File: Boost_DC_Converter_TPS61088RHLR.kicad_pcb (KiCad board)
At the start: 2 copper layers, 1 part, among them U1 TPS61088RHLR

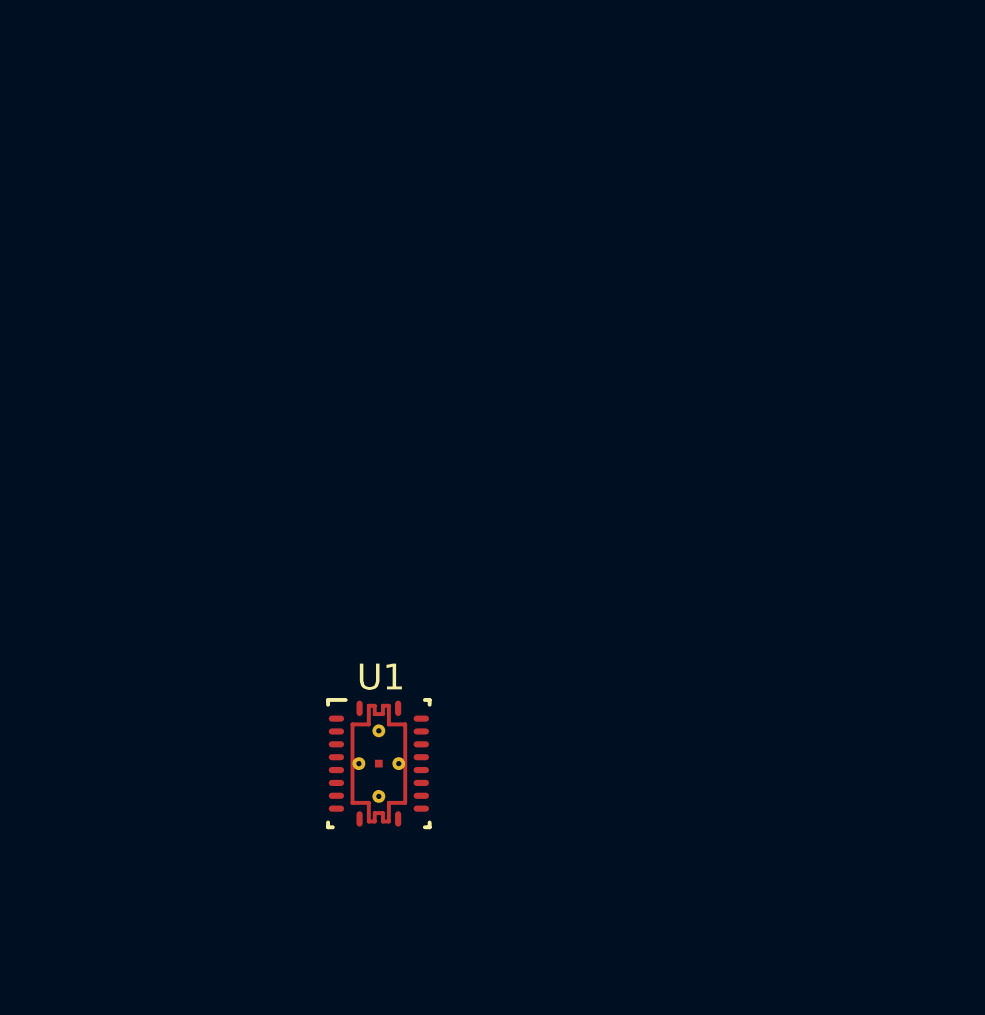
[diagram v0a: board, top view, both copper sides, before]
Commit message: Schematic done
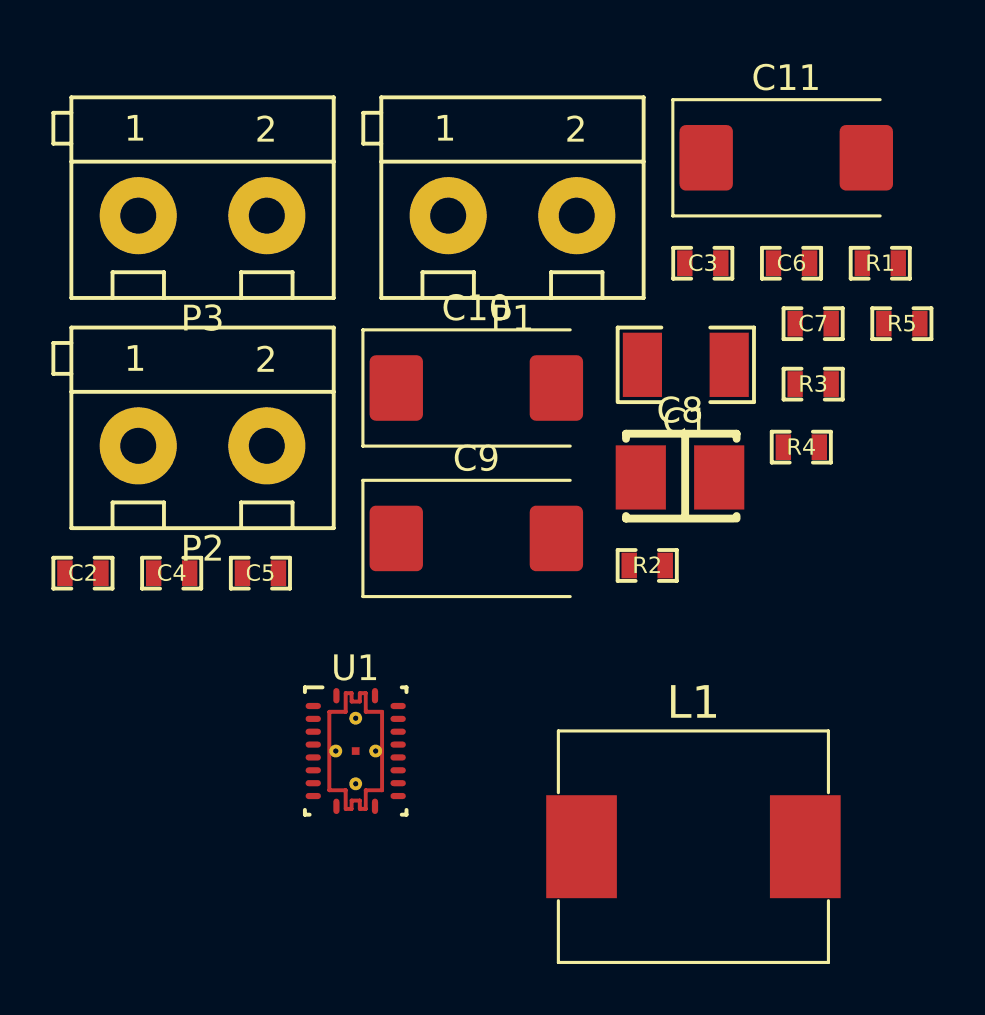
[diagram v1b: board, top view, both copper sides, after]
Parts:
- added C1: 10uF/35V, Capacitors_Smd_1210:10uF_35V_X7R_1210, F.Cu at (160.8, 83.5)
- added C10: 22uF/35V, Smd_Tantal:22uF_35V_Size_D, F.Cu at (152.6, 84.4)
- added C11: 22uF/35V, Smd_Tantal:22uF_35V_Size_D, F.Cu at (164.7, 75.5)
- added C2: 100nF/50V, Capacitors_Smd_0603:100nF_0603, F.Cu at (137.3, 91.6)
- added C3: 2n2F/50V, Capacitors_Smd_0603:2.2nF_0603, F.Cu at (161.4, 79.6)
- added C4: 220pF/50V, Capacitors_Smd_0603:220pF_0603, F.Cu at (140.8, 91.6)
- added C5: 47nF/50V, Capacitors_Smd_0603:47nF_0603, F.Cu at (144.2, 91.6)
- added C6: 2.2uF/6.3V, Capacitors_Smd_0603:2_2uF_0603, F.Cu at (164.9, 79.6)
- added C7: 100nF/50V, Capacitors_Smd_0603:100nF_0603, F.Cu at (165.7, 81.9)
- added C8: 1uF/35V, Smd_Tantal:1uF_35V_B_Tantal, F.Cu at (160.6, 87.9)
- added C9: 22uF/35V, Smd_Tantal:22uF_35V_Size_D, F.Cu at (152.6, 90.3)
- added L1: 1.2uH-12.9A, Inductors:CDMC8D28NP-1R2MC, F.Cu at (161.1, 102.2)
- added P1: DG301-5.0-02P-12-00A(H), Discrete_Connectors:DG301-5.0-02P-12-00A(H), F.Cu at (154.0, 77.7)
- added P2: DG301-5.0-02P-12-00A(H), Discrete_Connectors:DG301-5.0-02P-12-00A(H), F.Cu at (142.0, 86.7)
- added P3: DG301-5.0-02P-12-00A(H), Discrete_Connectors:DG301-5.0-02P-12-00A(H), F.Cu at (142.0, 77.7)
- added R1: 100k, Resistor_Smd_0603:100k_0603, F.Cu at (168.3, 79.6)
- added R2: 100k, Resistor_Smd_0603:100k_0603, F.Cu at (159.3, 91.3)
- added R3: 255k, Resistor_Smd_0603:255k_0603, F.Cu at (165.7, 84.3)
- added R4: 360k, Resistor_Smd_0603:360k_0603, F.Cu at (165.3, 86.7)
- added R5: 56k, Resistor_Smd_0603:56k_0603, F.Cu at (169.2, 81.9)
- moved U1 1.02 mm to (147.9, 98.5)
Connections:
- U1 pad 1: (no net) -> Net-(C6-Pad1)
- U1 pad 10: (no net) -> Net-(C5-Pad1)
- U1 pad 14: (no net) -> Net-(C10-Pad1)
- U1 pad 15: (no net) -> Net-(C10-Pad1)
- U1 pad 16: (no net) -> Net-(C10-Pad1)
- U1 pad 17: (no net) -> Net-(R4-Pad2)
- U1 pad 18: (no net) -> Net-(C4-Pad1)
- U1 pad 19: (no net) -> Net-(R2-Pad1)
- U1 pad 2: (no net) -> Net-(P2-Pad2)
- U1 pad 20: (no net) -> GND
- U1 pad 21: (no net) -> GND
- U1 pad 3: (no net) -> Net-(R3-Pad1)
- U1 pad 4: (no net) -> Net-(C7-Pad2)
- U1 pad 5: (no net) -> Net-(C7-Pad2)
- U1 pad 6: (no net) -> Net-(C7-Pad2)
- U1 pad 7: (no net) -> Net-(C7-Pad2)
- U1 pad 8: (no net) -> Net-(C7-Pad1)
- U1 pad 9: (no net) -> Net-(C1-Pad1)

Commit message: PCB almost done
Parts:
- added MH1: Mounting_Hole_M3_Grounded, Mounting_Holes:Mounting_Hole_M3_Grounded, F.Cu at (134.6, 56.9)
- added MH2: Mounting_Hole_M3_Grounded, Mounting_Holes:Mounting_Hole_M3_Grounded, F.Cu at (178.8, 56.9)
- added MH3: Mounting_Hole_M3_Grounded, Mounting_Holes:Mounting_Hole_M3_Grounded, F.Cu at (134.6, 40.0)
- added MH4: Mounting_Hole_M3_Grounded, Mounting_Holes:Mounting_Hole_M3_Grounded, F.Cu at (178.8, 40.1)
- moved C2 58.6 mm to (165.1, 40.0), turned to 90 degrees
- moved L1 53.0 mm to (169.8, 50.0), turned to 270 degrees
- moved U1 51.7 mm to (161.0, 48.5), turned to 180 degrees
- moved C5 49.5 mm to (160.9, 45.1), turned to 180 degrees
- moved C1 43.6 mm to (162.2, 40.0), turned to 90 degrees
- moved C9 42.0 mm to (149.3, 48.4), turned to 270 degrees
- moved C4 41.9 mm to (155.5, 52.4), turned to 270 degrees
- moved C8 41.6 mm to (153.7, 46.8), turned to 90 degrees
- moved R2 39.0 mm to (158.3, 52.4), turned to 270 degrees
- moved R4 38.8 mm to (157.8, 48.6), turned to 270 degrees
- moved P3 38.7 mm to (144.2, 39.1), turned to 180 degrees
- moved P1 38.6 mm to (154.2, 39.1), turned to 180 degrees
- moved C10 38.5 mm to (138.8, 48.5), turned to 270 degrees
- moved R5 35.7 mm to (156.2, 48.6), turned to 90 degrees
- moved C7 34.7 mm to (164.2, 47.3), turned to 270 degrees
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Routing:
- net GND: track 0.00 -> 77.6 mm, vias 0 -> 1
- net Net-(C7-Pad2): track 0.00 -> 36.4 mm
- net Net-(C10-Pad1): track 0.00 -> 35.6 mm
- net Net-(C1-Pad1): track 0.00 -> 28.7 mm
- net Net-(P2-Pad2): track 0.00 -> 21.2 mm
- net Net-(C4-Pad1): track 0.00 -> 5.04 mm
- net Net-(R4-Pad2): track 0.00 -> 3.19 mm
- net Net-(R3-Pad1): track 0.00 -> 1.89 mm
- net Net-(R2-Pad1): track 0.00 -> 1.89 mm
- net Net-(C7-Pad1): track 0.00 -> 1.86 mm
- net Net-(C3-Pad1): track 0.00 -> 1.23 mm
- added copper zone on B.Cu, net GND
- added copper zone on F.Cu, net GND
- added copper zone on F.Cu, net Net-(C1-Pad1)
- added copper zone on F.Cu, net Net-(C10-Pad1)
- added copper zone on F.Cu, net Net-(C7-Pad2)
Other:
- board outline added: 52.8 x 25.5 mm
- net class 8mils added: clearance 0.15, trace_width 0.2, via_dia 0.8, via_drill 0.4

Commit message: Added all tracks on pcb, problem with zones
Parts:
- U1: value TPS61088RHLR -> RHL0020A
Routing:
- net GND: track 77.6 -> 84.4 mm
- net Net-(C6-Pad1): track 0.00 -> 1.50 mm
- net Net-(C5-Pad1): track 0.00 -> 1.28 mm

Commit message: Generated gerbers and schematic BOM
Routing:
- net GND: track 84.4 -> 88.6 mm
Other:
- net class GND added: clearance 0.152, trace_width 0.127, via_dia 0.8, via_drill 0.4
- rule trace_min: 0.2 -> 0.1
- rule via_min_drill: 0.3 -> 0.1
- rule via_min_size: 0.4 -> 0.1
